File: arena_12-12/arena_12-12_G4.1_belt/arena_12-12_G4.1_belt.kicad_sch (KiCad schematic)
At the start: 0 parts

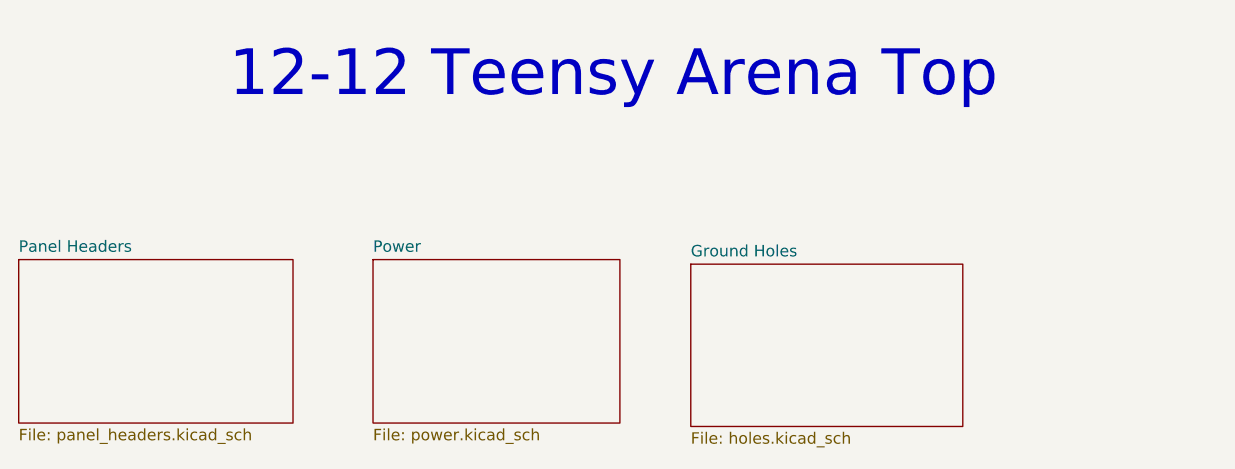
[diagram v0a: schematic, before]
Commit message: cleanup, belt with SMD power connector
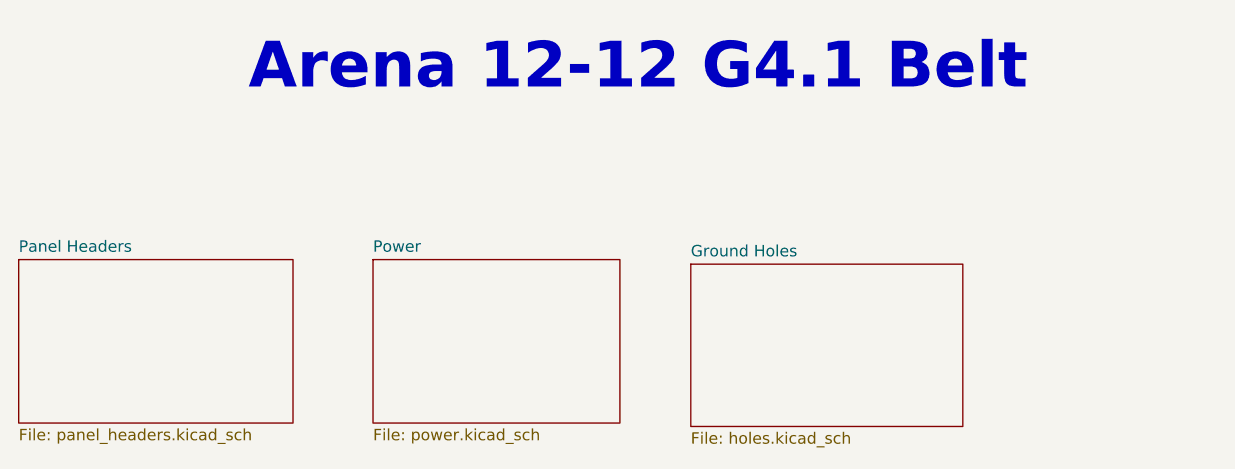
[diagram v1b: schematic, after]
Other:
- note added: "Arena 12-12 G4.1 Belt"
- note removed: "12-12 Teensy Arena Top"
- title: 12-12 Teensy G4.1 Arena Belt Modular LED Display -> Arena 12-12 G4.1 Belt :: Modular LED Display
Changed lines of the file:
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@@
 	(paper "User" 279.4 203.2)
 	(title_block
-		(title "12-12 Teensy G4.1 Arena Belt Modular LED Display")
-		(date "2025-07-22")
-		(rev "v0.5.1")
+		(title "Arena 12-12 G4.1 Belt :: Modular LED Display")
+		(date "2025-07-24")
+		(rev "v0.1")
 		(company "MCN-NET @ Janelia")
 	)
-	(text "12-12 Teensy Arena Top"
+	(text "Arena 12-12 G4.1 Belt"
 		(exclude_from_sim no)
-		(at 90.678 30.734 0)
+		(at 136.144 26.924 0)
 		(effects
 			(font
+				(face "KiCad Font")
 				(size 5.08 5.08)
+				(thickness 0.254)
+				(bold yes)
 			)
-			(justify left bottom)
 		)
 	)
@@
 		)
 		(instances
-			(project "arena_top_12-12"
+			(project "arena_12-12_G4.1_belt"
 				(path "/a2511654-3a17-43f1-8b9e-c45e375533dc"
 					(page "3")
@@
 		)
 		(instances
-			(project "arena_top_12-12"
+			(project "arena_12-12_G4.1_belt"
 				(path "/a2511654-3a17-43f1-8b9e-c45e375533dc"
 					(page "4")
@@
 		)
 		(instances
-			(project "arena_top_12-12"
+			(project "arena_12-12_G4.1_belt"
 				(path "/a2511654-3a17-43f1-8b9e-c45e375533dc"
 					(page "2")
